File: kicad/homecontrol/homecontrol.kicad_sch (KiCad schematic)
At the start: 72 parts, among them J1 Screw_Terminal_01x09, J2 Screw_Terminal_01x09, J3 Screw_Terminal_01x09, J4 Screw_Terminal_01x09, J5 AVR-ISP-10, U1 ATmega48P-20PU, U2 L7805ABP, U3 ULN2803A, U4 MAX232EEPE+, U5 A817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

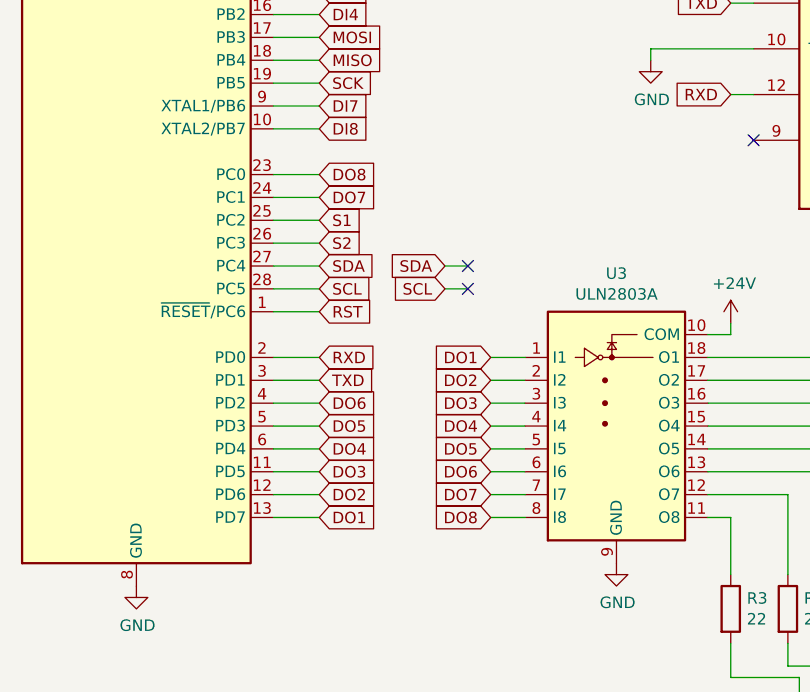
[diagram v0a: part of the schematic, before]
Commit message: Adapted IO mapping to new PCB layout
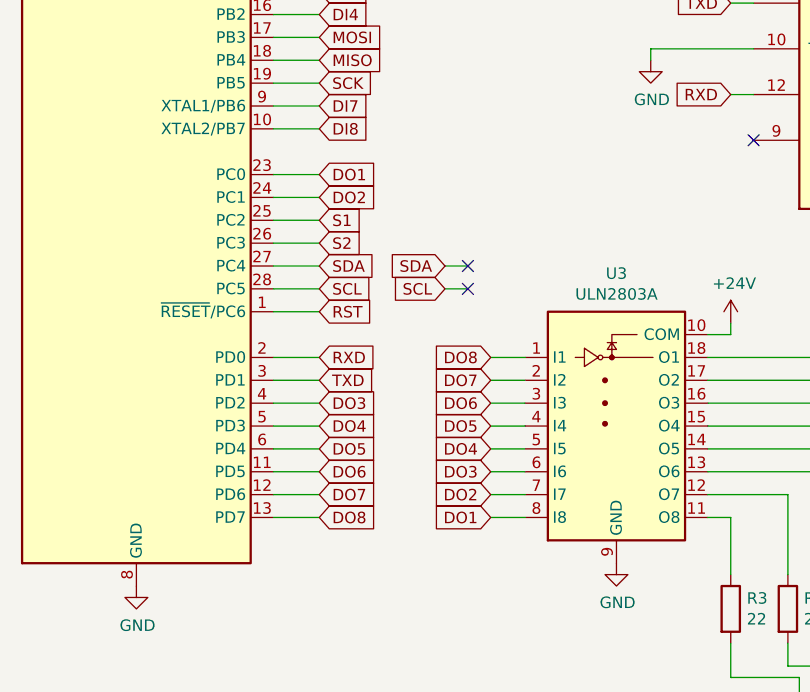
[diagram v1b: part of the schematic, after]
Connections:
- net DO1: now also U1.23 (PC0), U3.8 (I8); no longer U1.13 (PD7), U3.1 (I1)
- net DO2: now also U1.24 (PC1), U3.7 (I7); no longer U1.12 (PD6), U3.2 (I2)
- net DO3: now also U1.4 (PD2), U3.6 (I6); no longer U1.11 (PD5), U3.3 (I3)
- net DO4: now also U1.5 (PD3), U3.5 (I5); no longer U1.6 (PD4), U3.4 (I4)
- net DO5: now also U1.6 (PD4), U3.4 (I4); no longer U1.5 (PD3), U3.5 (I5)
- net DO6: now also U1.11 (PD5), U3.3 (I3); no longer U1.4 (PD2), U3.6 (I6)
- net DO7: now also U1.12 (PD6), U3.2 (I2); no longer U1.24 (PC1), U3.7 (I7)
- net DO8: now also U1.13 (PD7), U3.1 (I1); no longer U1.23 (PC0), U3.8 (I8)
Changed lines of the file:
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@@
     (effects (font (size 1.27 1.27)) (justify right bottom))
   )
-  (global_label "DO5" (shape input) (at 91.44 154.94 180)
+  (global_label "DO4" (shape input) (at 91.44 154.94 180)
     (effects (font (size 1.27 1.27)) (justify right))
     (property "Intersheetrefs" "${INTERSHEET_REFS}" (at 91.44 154.94 0)
@@
     )
   )
-  (global_label "DO6" (shape input) (at 91.44 157.48 180)
+  (global_label "DO3" (shape input) (at 91.44 157.48 180)
     (effects (font (size 1.27 1.27)) (justify right))
     (property "Intersheetrefs" "${INTERSHEET_REFS}" (at 91.44 157.48 0)
@@
     )
   )
-  (global_label "DO5" (shape input) (at 72.39 152.4 0)
+  (global_label "DO4" (shape input) (at 72.39 152.4 0)
     (effects (font (size 1.27 1.27)) (justify left))
     (property "Intersheetrefs" "${INTERSHEET_REFS}" (at 72.39 152.4 0)
@@
     )
   )
-  (global_label "DO8" (shape input) (at 91.44 162.56 180)
+  (global_label "DO1" (shape input) (at 91.44 162.56 180)
     (effects (font (size 1.27 1.27)) (justify right))
     (property "Intersheetrefs" "${INTERSHEET_REFS}" (at 91.44 162.56 0)
@@
     )
   )
-  (global_label "DO4" (shape input) (at 91.44 152.4 180)
+  (global_label "DO5" (shape input) (at 91.44 152.4 180)
     (effects (font (size 1.27 1.27)) (justify right))
     (property "Intersheetrefs" "${INTERSHEET_REFS}" (at 91.44 152.4 0)
@@
     )
   )
-  (global_label "DO6" (shape input) (at 72.39 149.86 0)
+  (global_label "DO3" (shape input) (at 72.39 149.86 0)
     (effects (font (size 1.27 1.27)) (justify left))
     (property "Intersheetrefs" "${INTERSHEET_REFS}" (at 72.39 149.86 0)
@@
     )
   )
-  (global_label "DO2" (shape input) (at 91.44 147.32 180)
+  (global_label "DO7" (shape input) (at 91.44 147.32 180)
     (effects (font (size 1.27 1.27)) (justify right))
     (property "Intersheetrefs" "${INTERSHEET_REFS}" (at 91.44 147.32 0)
@@
     )
   )
-  (global_label "DO1" (shape input) (at 72.39 162.56 0)
+  (global_label "DO8" (shape input) (at 72.39 162.56 0)
     (effects (font (size 1.27 1.27)) (justify left))
     (property "Intersheetrefs" "${INTERSHEET_REFS}" (at 72.39 162.56 0)
@@
     )
   )
-  (global_label "DO3" (shape input) (at 91.44 149.86 180)
+  (global_label "DO6" (shape input) (at 91.44 149.86 180)
     (effects (font (size 1.27 1.27)) (justify right))
     (property "Intersheetrefs" "${INTERSHEET_REFS}" (at 91.44 149.86 0)
@@
     )
   )
-  (global_label "DO4" (shape input) (at 72.39 154.94 0)
+  (global_label "DO5" (shape input) (at 72.39 154.94 0)
     (effects (font (size 1.27 1.27)) (justify left))
     (property "Intersheetrefs" "${INTERSHEET_REFS}" (at 72.39 154.94 0)
@@
     )
   )
-  (global_label "DO3" (shape input) (at 72.39 157.48 0)
+  (global_label "DO6" (shape input) (at 72.39 157.48 0)
     (effects (font (size 1.27 1.27)) (justify left))
     (property "Intersheetrefs" "${INTERSHEET_REFS}" (at 72.39 157.48 0)
@@
     )
   )
-  (global_label "DO8" (shape input) (at 72.39 124.46 0)
+  (global_label "DO1" (shape input) (at 72.39 124.46 0)
     (effects (font (size 1.27 1.27)) (justify left))
     (property "Intersheetrefs" "${INTERSHEET_REFS}" (at 72.39 124.46 0)
@@
     )
   )
-  (global_label "DO7" (shape input) (at 72.39 127 0)
+  (global_label "DO2" (shape input) (at 72.39 127 0)
     (effects (font (size 1.27 1.27)) (justify left))
     (property "Intersheetrefs" "${INTERSHEET_REFS}" (at 72.39 127 0)
@@
     )
   )
-  (global_label "DO7" (shape input) (at 91.44 160.02 180)
+  (global_label "DO2" (shape input) (at 91.44 160.02 180)
     (effects (font (size 1.27 1.27)) (justify right))
     (property "Intersheetrefs" "${INTERSHEET_REFS}" (at 91.44 160.02 0)
@@
     )
   )
-  (global_label "DO1" (shape input) (at 91.44 144.78 180)
+  (global_label "DO8" (shape input) (at 91.44 144.78 180)
     (effects (font (size 1.27 1.27)) (justify right))
     (property "Intersheetrefs" "${INTERSHEET_REFS}" (at 91.44 144.78 0)
@@
     )
   )
-  (global_label "DO2" (shape input) (at 72.39 160.02 0)
+  (global_label "DO7" (shape input) (at 72.39 160.02 0)
     (effects (font (size 1.27 1.27)) (justify left))
     (property "Intersheetrefs" "${INTERSHEET_REFS}" (at 72.39 160.02 0)
